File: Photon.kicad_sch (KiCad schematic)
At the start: 1 part

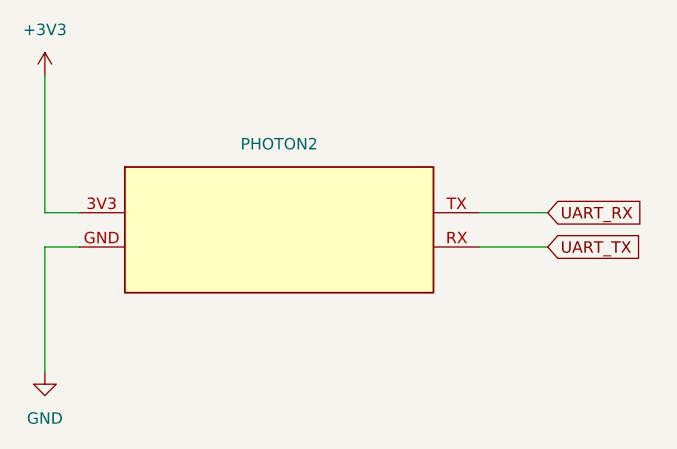
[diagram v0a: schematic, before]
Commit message: Connecteur AVR + Branchement MOSI/MISO/SCK + CS
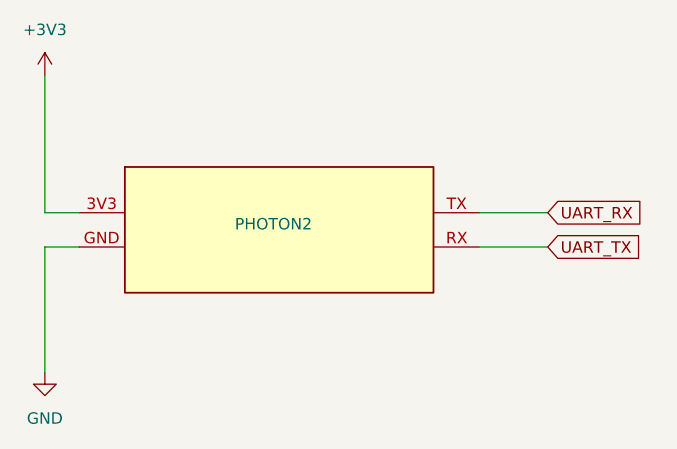
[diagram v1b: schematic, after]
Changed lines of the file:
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@@
   )
   (symbol (lib_id "New_Library:Photon2") (at 140.97 116.84 0) (unit 1)
-    (in_bom yes) (on_board yes) (dnp no) (fields_autoplaced)
-    (property "Reference" "PHOTON2" (at 142.875 85.09 0)
+    (in_bom yes) (on_board yes) (dnp no)
+    (property "Reference" "PHOTON2" (at 142.24 93.98 0)
       (effects (font (size 1.27 1.27)))
     )
